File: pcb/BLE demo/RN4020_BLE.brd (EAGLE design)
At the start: 39.7 x 34.9 mm, 20 parts, among them U1 PIC18LF25K50-I/SO, U2 TC1262_VDB

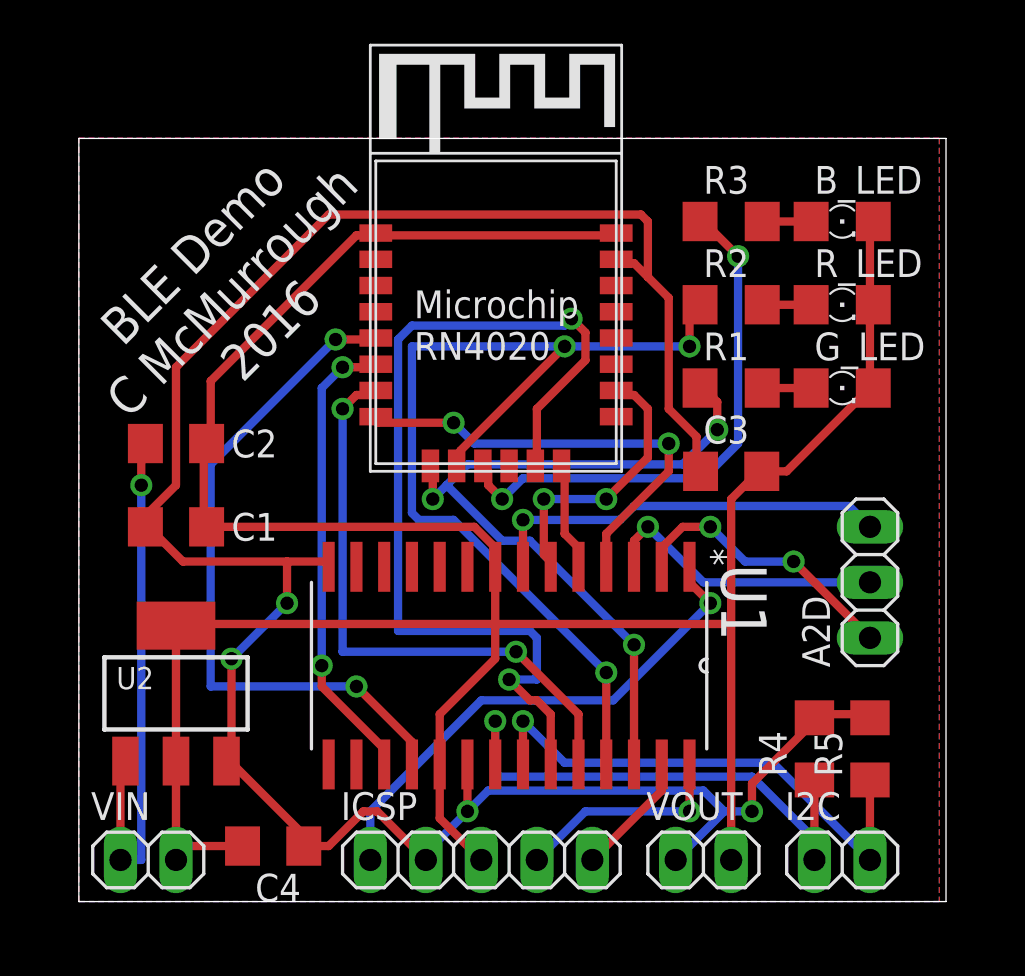
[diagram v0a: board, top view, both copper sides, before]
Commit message: fixed BLE PCB, removed version from file name
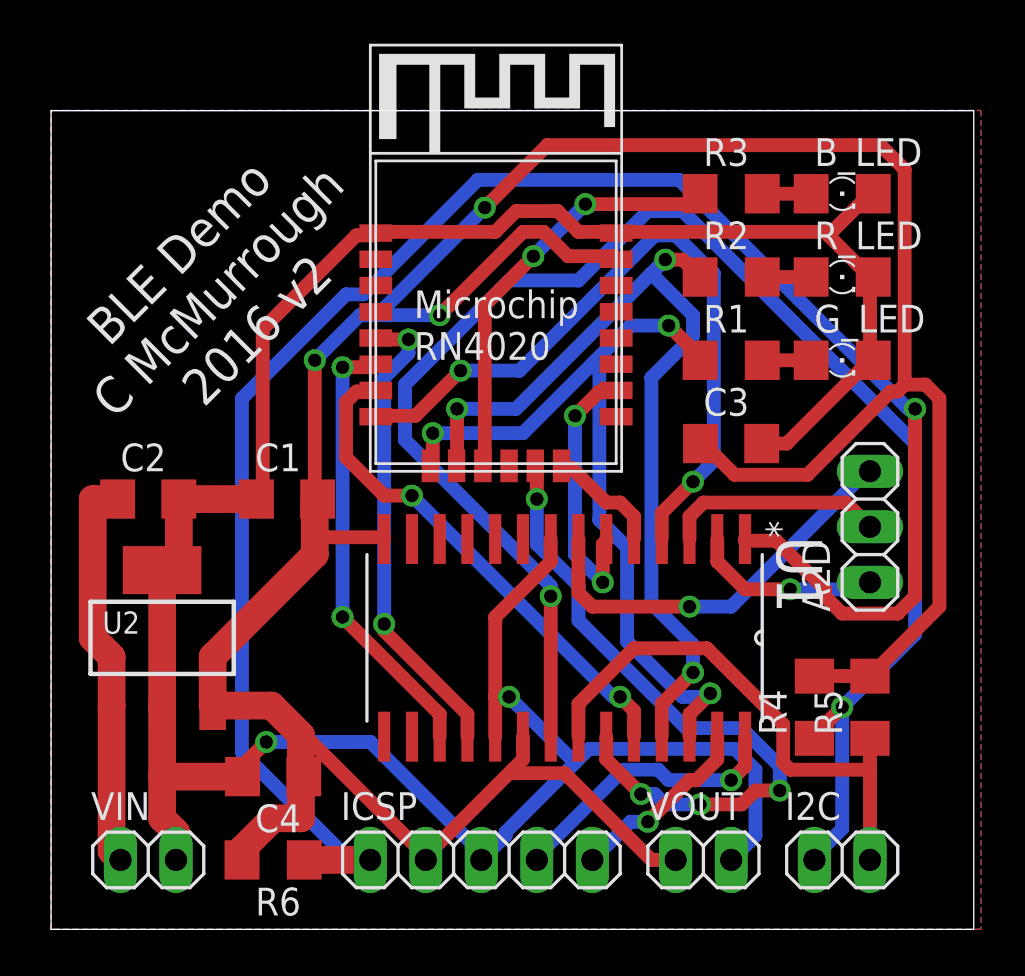
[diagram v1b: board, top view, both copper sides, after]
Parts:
- added R6: 4.7k, resistor:R1206
- moved C1 5.24 mm to (8.89, 17.8), turned to 180 degrees
- moved C4 3.17 mm to (8.26, 5.08)
- moved C2 2.84 mm to (2.54, 17.8)
- moved U1 2.84 mm to (21.6, 11.4)
- moved U2 2.62 mm to (3.17, 11.4)
- moved A2D 2.54 mm to (35.6, 16.5)
- moved R4 1.91 mm to (33.0, 8.26)
- moved R5 1.91 mm to (35.6, 8.26)
- moved B_LED 1.27 mm to (34.3, 31.8)
- moved C3 1.27 mm to (29.2, 20.3)
- moved G_LED 1.27 mm to (34.3, 24.1)
- moved R1 1.27 mm to (29.2, 24.1)
- moved R2 1.27 mm to (29.2, 27.9)
- moved R3 1.27 mm to (29.2, 31.8)
- moved R_LED 1.27 mm to (34.3, 27.9)
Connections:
- net +3V3: now also R6.2
- net MCLR: now also R6.1
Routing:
- net MCLR: track 23.8 -> 84.7 mm
- net SDA: track 24.9 -> 72.8 mm, vias 1 -> 2
- net +3V3: track 109.4 -> 142.4 mm, vias 4 -> 3
- net BT_UART_CTS: track 44.1 -> 31.1 mm, vias 2 -> 4
- net CMD/MLDP: track 20.8 -> 32.8 mm
- net BT_UART_TX: track 31.4 -> 21.7 mm
- net N$4: track 24.9 -> 18.2 mm, vias 1 -> 0
- net PIO3: track 24.7 -> 19.4 mm
- net PIO2: track 46.2 -> 41.0 mm
- net GND: track 130.8 -> 126.1 mm, vias 0 -> 2
- net AN0: track 12.9 -> 8.67 mm, vias 2 -> 1
- net SWAKE: track 27.2 -> 23.3 mm
- net AN1: track 13.3 -> 10.0 mm, vias 1 -> 0
- net PGD: track 10.1 -> 13.1 mm
- net PGC: track 5.68 -> 8.66 mm, vias 0 -> 1
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- added copper zone on layer 16, net N$5
- added copper zone on layer 1, net N$9
- removed copper zone on layer 1, net GND
- removed copper zone on layer 16, net GND
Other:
- board size 39.7 x 34.9 mm -> 42.2 x 37.5 mm
- board text added: "BLE Demo C McMurrough 2016 v2"
- board text removed: "BLE Demo C McMurrough 2016"
